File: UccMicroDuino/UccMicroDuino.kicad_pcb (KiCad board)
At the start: 2 copper layers, 45 x 45 mm, 14 parts, among them J1 Pcb USB type A, J2 Header, U1 ATtiny85-20S

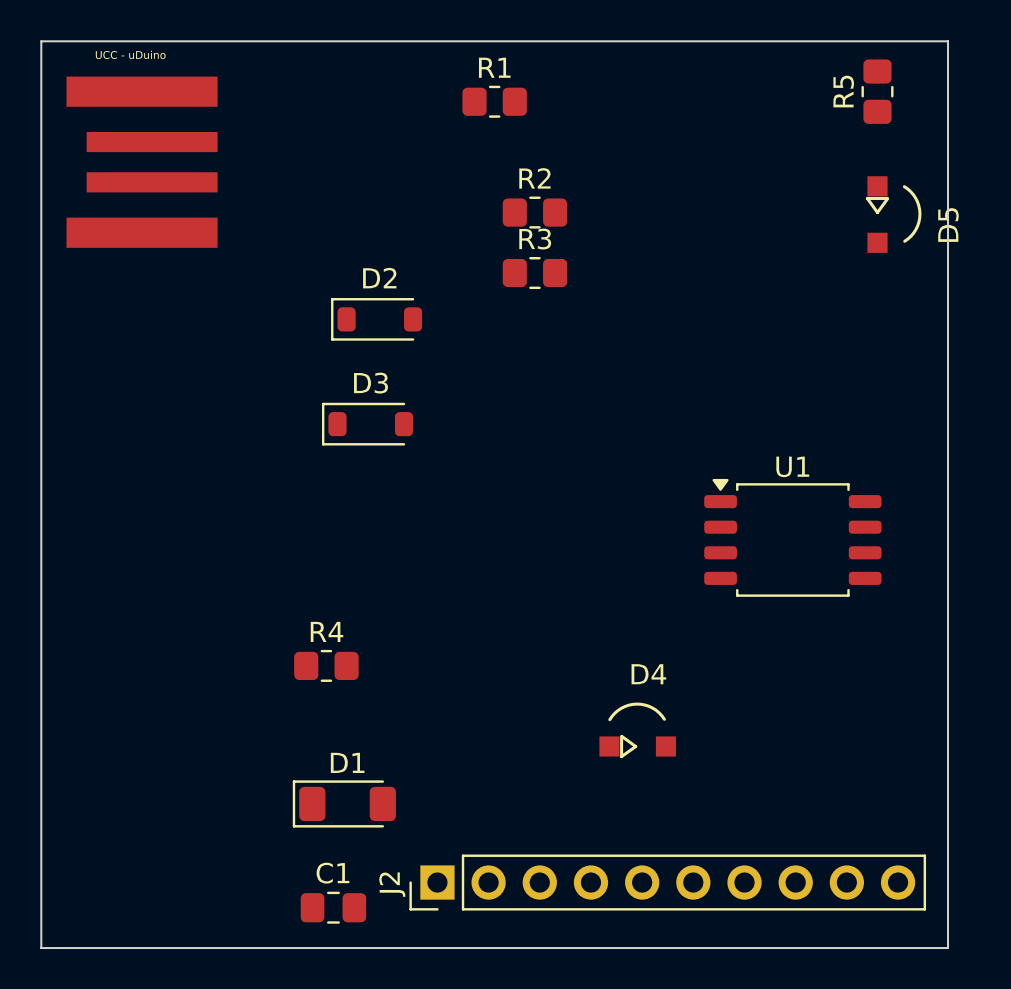
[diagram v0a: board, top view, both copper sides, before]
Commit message: PCB: Ruteo Completo, 0 errores
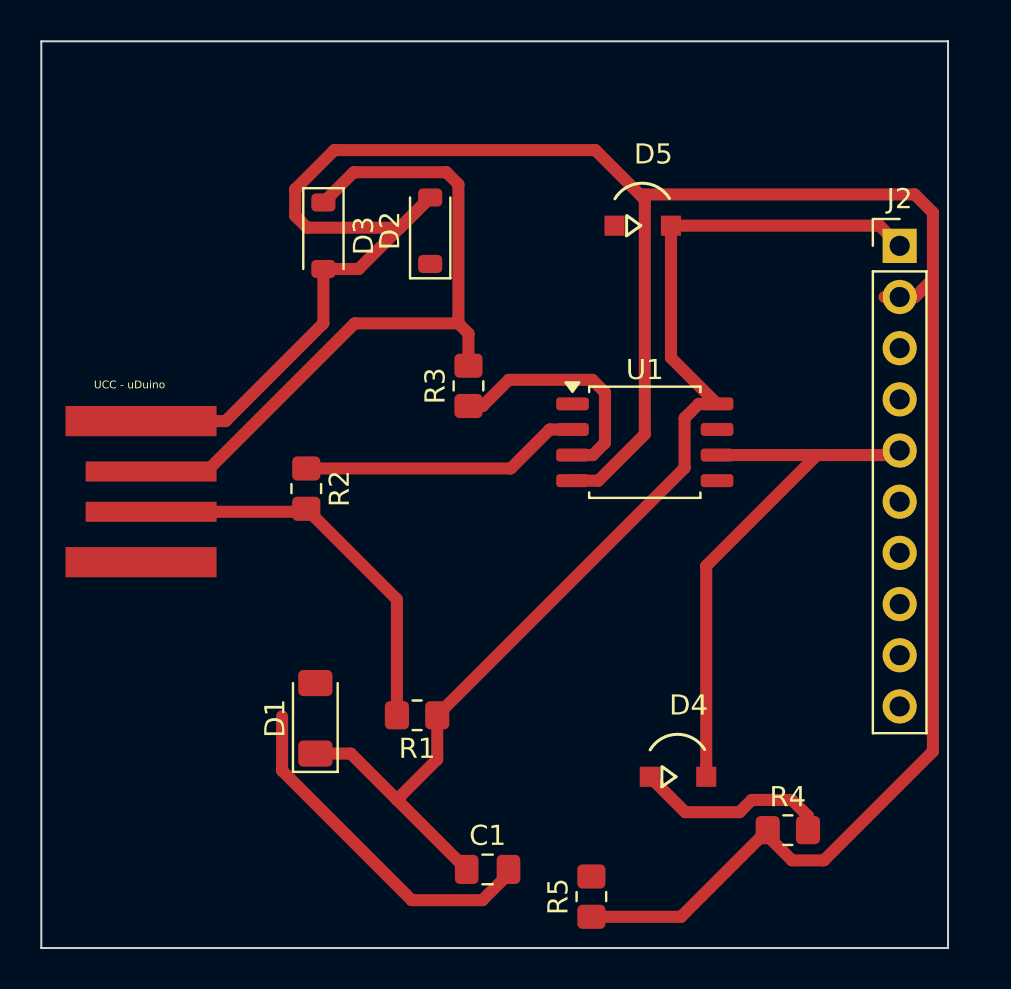
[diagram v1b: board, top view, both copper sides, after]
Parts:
- moved R5 42.4 mm to (208.3, 110.0)
- moved J2 39.0 mm to (223.6, 77.7), turned to 0 degrees
- moved R1 30.7 mm to (199.7, 101.0), turned to 180 degrees
- moved R4 24.3 mm to (218.1, 106.7)
- moved R2 17.8 mm to (194.2, 89.7), turned to -90 degrees
- moved J1 16.4 mm to (186.2, 89.8)
- moved D5 11.3 mm to (211.2, 76.7), turned to 0 degrees
- moved D3 9.64 mm to (195.0, 77.2), turned to -90 degrees
- moved U1 8.81 mm to (210.9, 87.4)
- moved C1 7.88 mm to (203.2, 108.6)
- moved R3 6.50 mm to (202.2, 84.6), turned to 90 degrees
- moved D2 5.06 mm to (200.3, 76.9), turned to 90 degrees
- moved D1 4.54 mm to (194.6, 101.1), turned to 90 degrees
- moved D4 2.50 mm to (213.0, 104.0)
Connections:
- C1 pad 2: (no net) -> GND
- D1 pad 2: (no net) -> Net-(D1-A)
- D2 pad 1: (no net) -> Net-(D2-K)
- D5 pad 1: (no net) -> Net-(D5-K)
- J2 pad 10: (no net) -> unconnected-(J2-Pin_10-Pad10)
- J2 pad 3: (no net) -> unconnected-(J2-Pin_3-Pad3)
- J2 pad 4: (no net) -> Net-(J2-Pin_4)
- J2 pad 6: (no net) -> Net-(J2-Pin_6)
- J2 pad 7: (no net) -> Net-(J2-Pin_7)
- J2 pad 8: (no net) -> Net-(J2-Pin_8)
- J2 pad 9: (no net) -> Net-(J2-Pin_9)
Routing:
- net GND: track 0.00 -> 148.3 mm
- net +5V: track 0.00 -> 58.2 mm
- net Net-(D3-K): track 0.00 -> 35.1 mm
- net Net-(D4-A): track 0.00 -> 28.0 mm
- net Net-(D2-K): track 0.00 -> 19.9 mm
- net Net-(J2-Pin_7): track 0.00 -> 14.0 mm
- net Net-(J2-Pin_8): track 0.00 -> 11.9 mm
- net Net-(D4-K): track 0.00 -> 9.86 mm
